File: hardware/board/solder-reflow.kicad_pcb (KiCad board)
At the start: 2 copper layers, 128.3 x 63.5 mm, 55 parts, among them J1 AC_Con, J2 OLED 0.91, J3 PTC_Con, J4 Barrel_Jack_Switch_Pin3Ring, K1 G3MB202PDC12, Q1 BC557, SW1 RotaryEncoder_Switch, U1 TL431LP, U2 OPA2134, U3 OPA2134, U4 L7805, U5 WeMos_D1_mini

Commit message: [6-7-1245] finish first layout, need to review
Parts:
- removed C4, C5: 10nF, Capacitor_THT:C_Disc_D4.3mm_W1.9mm_P5.00mm
- removed H3: MountingHole_Pad, MountingHole:MountingHole_3.2mm_M3_DIN965_Pad
- removed R11, R21: 10k, Resistor_THT:R_Axial_DIN0207_L6.3mm_D2.5mm_P10.16mm_Horizontal
- removed REF**: OSHW-Logo2_14.6x12mm_Copper, Symbol:OSHW-Logo2_14.6x12mm_Copper
- removed REF** (x2): ESD-Logo_8.9x8mm_SilkScreen, Symbol:ESD-Logo_8.9x8mm_SilkScreen
- removed REF**: Gauge_10mm_Type5_SilkScreenTop, Calibration_Scale:Gauge_10mm_Type5_SilkScreenTop
- removed SW1: RotaryEncoder_Switch, Rotary_Encoder:RotaryEncoder_Alps_EC11E-Switch_Vertical_H20mm
- removed U5: WeMos_D1_mini, Module:WEMOS_D1_mini_light
- added C10: 100nF, Capacitor_SMD:C_1206_3216Metric_Pad1.33x1.80mm_HandSolder, F.Cu at (128.5, 81.5)
- added C11: 100nF, Capacitor_SMD:C_1206_3216Metric_Pad1.33x1.80mm_HandSolder, B.Cu at (141.6, 77.0)
- added C12: 100nF, Capacitor_SMD:C_1206_3216Metric_Pad1.33x1.80mm_HandSolder, B.Cu at (150.1, 77.0)
- added C13: 22uF, Capacitor_SMD:C_1206_3216Metric_Pad1.33x1.80mm_HandSolder, B.Cu at (147.1, 77.0)
- added C14: 100nF, Capacitor_SMD:C_1206_3216Metric_Pad1.33x1.80mm_HandSolder, B.Cu at (110.2, 81.0)
- added C15: 100nF, Capacitor_SMD:C_1206_3216Metric_Pad1.33x1.80mm_HandSolder, B.Cu at (122.0, 81.0)
- added C16: 1uF, Capacitor_SMD:C_1206_3216Metric_Pad1.33x1.80mm_HandSolder, B.Cu at (117.0, 89.5)
- added C17: 1uF, Capacitor_SMD:C_1206_3216Metric_Pad1.33x1.80mm_HandSolder, B.Cu at (117.0, 98.0)
- added C18: 1uF, Capacitor_SMD:C_1206_3216Metric_Pad1.33x1.80mm_HandSolder, B.Cu at (117.0, 106.5)
- added C19: 1uF, Capacitor_SMD:C_1206_3216Metric_Pad1.33x1.80mm_HandSolder, B.Cu at (117.0, 114.9)
- added C8: 22uF, Capacitor_SMD:C_1206_3216Metric_Pad1.33x1.80mm_HandSolder, B.Cu at (159.9, 95.8)
- added C9: 22uF, Capacitor_SMD:C_1206_3216Metric_Pad1.33x1.80mm_HandSolder, B.Cu at (156.9, 95.8)
- added D4: 1N4001, Diode_SMD:D_SOD-123, F.Cu at (174.2, 94.8)
- added D5: SSR2, LED_SMD:LED_2010_5025Metric_Pad1.52x2.65mm_HandSolder, F.Cu at (156.6, 107.7)
- added D7: TXD, LED_SMD:LED_2010_5025Metric_Pad1.52x2.65mm_HandSolder, F.Cu at (160.1, 91.0)
- added D8: RXD, LED_SMD:LED_2010_5025Metric_Pad1.52x2.65mm_HandSolder, F.Cu at (160.1, 100.0)
- added J10: PINOUT, Connector_PinHeader_2.54mm:PinHeader_1x10_P2.54mm_Vertical, F.Cu at (165.1, 76.1)
- added J12: ST7789, Connector_PinSocket_2.54mm:PinSocket_1x07_P2.54mm_Vertical, F.Cu at (139.5, 101.5)
- added J13: JTAG10, Connector_PinHeader_2.54mm:PinHeader_2x05_P2.54mm_Vertical, F.Cu at (141.2, 109.8)
- added J5: SSROUT2, TerminalBlock_MetzConnect:TerminalBlock_MetzConnect_Type011_RT05502HBWC_1x02_P5.00mm_Horizontal, F.Cu at (182.7, 108.2)
- added J6: USB_B, Connector_USB:USB_B_OST_USB-B1HSxx_Horizontal, F.Cu at (112.0, 74.5)
- added J7: PINOUT, Connector_PinHeader_2.54mm:PinHeader_1x10_P2.54mm_Vertical, F.Cu at (136.3, 116.2)
- added J8: PINOUT, Connector_PinHeader_2.54mm:PinHeader_1x10_P2.54mm_Vertical, F.Cu at (132.1, 76.2)
- added J9: 12VIN, TerminalBlock_MetzConnect:TerminalBlock_MetzConnect_Type011_RT05502HBWC_1x02_P5.00mm_Horizontal, F.Cu at (182.8, 86.0)
- added Q2: SS8550, Package_TO_SOT_SMD:SOT-23_Handsoldering, F.Cu at (169.2, 94.5)
- added Q3: SS8050, Package_TO_SOT_SMD:SOT-23_Handsoldering, F.Cu at (127.0, 89.5)
- added Q4: SS8050, Package_TO_SOT_SMD:SOT-23_Handsoldering, F.Cu at (127.0, 97.0)
- added R23: 10k, Resistor_SMD:R_0805_2012Metric_Pad1.20x1.40mm_HandSolder, F.Cu at (168.5, 89.5)
- added R24: 10k, Resistor_SMD:R_0805_2012Metric_Pad1.20x1.40mm_HandSolder, F.Cu at (171.4, 89.5)
- added R25: 1k, Resistor_SMD:R_0805_2012Metric_Pad1.20x1.40mm_HandSolder, F.Cu at (174.5, 89.5)
- added R26: 1k, Resistor_SMD:R_0805_2012Metric_Pad1.20x1.40mm_HandSolder, B.Cu at (157.2, 84.2)
- added R27: 1k, Resistor_SMD:R_0805_2012Metric_Pad1.20x1.40mm_HandSolder, B.Cu at (159.8, 84.2)
- added R28: 1k, Resistor_SMD:R_0805_2012Metric_Pad1.20x1.40mm_HandSolder, B.Cu at (144.3, 76.3)
- added R29: 22k, Resistor_SMD:R_0805_2012Metric_Pad1.20x1.40mm_HandSolder, B.Cu at (128.5, 87.5)
- added R30: 22k, Resistor_SMD:R_0805_2012Metric_Pad1.20x1.40mm_HandSolder, B.Cu at (127.1, 82.0)
- added R31: 22k, Resistor_SMD:R_0805_2012Metric_Pad1.20x1.40mm_HandSolder, B.Cu at (127.5, 77.0)
- added R32: 22k, Resistor_SMD:R_0805_2012Metric_Pad1.20x1.40mm_HandSolder, B.Cu at (128.5, 96.0)
- added RA1: 25k, Resistor_SMD:R_0805_2012Metric_Pad1.20x1.40mm_HandSolder, F.Cu at (126.5, 109.5)
- added RB1: 25k, Resistor_SMD:R_0805_2012Metric_Pad1.20x1.40mm_HandSolder, F.Cu at (126.5, 112.0)
- added SW2: RST, Button_Switch_SMD:SW_SPST_B3S-1000, F.Cu at (110.2, 81.0)
- added SW3: IO0, Button_Switch_SMD:SW_SPST_B3S-1000, F.Cu at (122.0, 81.0)
- added SW4: IO0, Button_Switch_SMD:SW_SPST_B3S-1000, F.Cu at (117.0, 89.5)
- added SW5: IO0, Button_Switch_SMD:SW_SPST_B3S-1000, F.Cu at (117.0, 98.0)
- added SW6: IO0, Button_Switch_SMD:SW_SPST_B3S-1000, F.Cu at (117.0, 106.5)
- added SW7: IO0, Button_Switch_SMD:SW_SPST_B3S-1000, F.Cu at (117.0, 114.9)
- added U6: ESP32-WROOM-32D, RF_Module:ESP32-WROOM-32D, F.Cu at (147.1, 83.5)
- added U7: CH340C, Package_SO:SOIC-16_3.9x9.9mm_P1.27mm, B.Cu at (138.0, 85.5)
- C1: value 68nF -> 1nF; footprint Capacitor_THT:C_Disc_D4.3mm_W1.9mm_P5.00mm -> Capacitor_SMD:C_1206_3216Metric_Pad1.33x1.80mm_HandSolder
- C2: value 390nF -> 1uF; footprint Capacitor_THT:C_Disc_D4.3mm_W1.9mm_P5.00mm -> Capacitor_SMD:C_1206_3216Metric_Pad1.33x1.80mm_HandSolder; moved to B.Cu
- C3: value 180nF -> 1nF; footprint Capacitor_THT:C_Disc_D4.3mm_W1.9mm_P5.00mm -> Capacitor_SMD:C_1206_3216Metric_Pad1.33x1.80mm_HandSolder
- C6, C7: footprint Capacitor_THT:CP_Radial_D6.3mm_P2.50mm -> Capacitor_SMD:C_1206_3216Metric_Pad1.33x1.80mm_HandSolder; moved to B.Cu
- D1: footprint Diode_THT:D_DO-41_SOD81_P10.16mm_Horizontal -> Diode_SMD:D_SOD-123; moved to B.Cu
- D2: value SSR -> SSR1; footprint LED_THT:LED_D5.0mm -> LED_SMD:LED_2010_5025Metric_Pad1.52x2.65mm_HandSolder
- D3: footprint LED_THT:LED_D5.0mm -> LED_SMD:LED_2010_5025Metric_Pad1.52x2.65mm_HandSolder
- F1, K1, TH1, U4: moved to B.Cu
- J1: value AC_Con -> ACCON; footprint TerminalBlock_MetzConnect:TerminalBlock_MetzConnect_Type011_RT05502HBWC_1x02_P5.00mm_Horizontal -> TerminalBlock_MetzConnect:TerminalBlock_MetzConnect_Type055_RT01503HDWU_1x03_P5.00mm_Horizontal
- J4: value Barrel_Jack_Switch_Pin3Ring -> 12V
- Q1: value BC557 -> SS8550; footprint Package_TO_SOT_THT:TO-92_Inline_Wide -> Package_TO_SOT_SMD:SOT-23_Handsoldering; moved to B.Cu
- R1, R14, R15, R16, R17, R18, R19, R2, R20, R4, R5, R6: footprint Resistor_THT:R_Axial_DIN0207_L6.3mm_D2.5mm_P10.16mm_Horizontal -> Resistor_SMD:R_0805_2012Metric_Pad1.20x1.40mm_HandSolder; moved to B.Cu
- R10: value 5.1K -> 10k; footprint Resistor_THT:R_Axial_DIN0207_L6.3mm_D2.5mm_P10.16mm_Horizontal -> Resistor_SMD:R_0805_2012Metric_Pad1.20x1.40mm_HandSolder
- R12: value 3.09k -> 4K7; footprint Resistor_THT:R_Axial_DIN0207_L6.3mm_D2.5mm_P10.16mm_Horizontal -> Resistor_SMD:R_0805_2012Metric_Pad1.20x1.40mm_HandSolder; moved to B.Cu
- R13: value 20k -> 4K7; footprint Resistor_THT:R_Axial_DIN0207_L6.3mm_D2.5mm_P10.16mm_Horizontal -> Resistor_SMD:R_0805_2012Metric_Pad1.20x1.40mm_HandSolder; moved to B.Cu
- R22, R3: footprint Resistor_THT:R_Axial_DIN0207_L6.3mm_D2.5mm_P10.16mm_Horizontal -> Resistor_SMD:R_0805_2012Metric_Pad1.20x1.40mm_HandSolder
- R7: value 1k -> 10k; footprint Resistor_THT:R_Axial_DIN0207_L6.3mm_D2.5mm_P10.16mm_Horizontal -> Resistor_SMD:R_0805_2012Metric_Pad1.20x1.40mm_HandSolder
- R8: value 17.4k -> 16k; footprint Resistor_THT:R_Axial_DIN0207_L6.3mm_D2.5mm_P10.16mm_Horizontal -> Resistor_SMD:R_0805_2012Metric_Pad1.20x1.40mm_HandSolder
- R9: value 107k -> 16k; footprint Resistor_THT:R_Axial_DIN0207_L6.3mm_D2.5mm_P10.16mm_Horizontal -> Resistor_SMD:R_0805_2012Metric_Pad1.20x1.40mm_HandSolder
- U2: value OPA2134 -> TL074; footprint Package_DIP:DIP-8_W7.62mm_LongPads -> Package_SO:SOIC-14_3.9x8.7mm_P1.27mm; moved to B.Cu
- U3: value OPA2134 -> AMS1117-3.3; footprint Package_DIP:DIP-8_W7.62mm_LongPads -> Package_TO_SOT_SMD:SOT-223-3_TabPin2; moved to B.Cu
- moved J3 84.4 mm to (182.7, 97.2)
- moved H4 75.4 mm to (169.5, 117.0)
- moved TH1 75.3 mm to (165.2, 102.0)
- moved R1 54.0 mm to (126.6, 111.0), turned to 180 degrees
- moved C1 53.8 mm to (131.8, 105.0), turned to -90 degrees
- moved R13 53.3 mm to (145.1, 87.0), turned to 180 degrees
- moved R8 52.4 mm to (126.5, 104.5), turned to 180 degrees
- moved R12 50.0 mm to (145.1, 89.5), turned to 180 degrees
- moved U3 48.8 mm to (152.2, 85.8), turned to 90 degrees
- moved U2 48.3 mm to (133.5, 106.5), turned to 180 degrees
- moved H2 46.7 mm to (171.5, 78.5)
- moved J1 46.6 mm to (183.0, 125.8), turned to 90 degrees
- moved C7 45.3 mm to (157.6, 89.2), turned to -90 degrees
- moved R4 45.2 mm to (126.6, 106.0), turned to 180 degrees
- moved R3 44.1 mm to (126.5, 102.0), turned to 180 degrees
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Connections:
- net /pt100_out renamed /PT100Voltage
- net Net-(U4-IN) renamed +12V
- C1 pad 1: Net-(C1-Pad1) -> Net-(U2D-+)
- C2 pad 1: Net-(C1-Pad2) -> +3.3V
- C3 pad 1: Net-(U3A-+) -> Net-(U2C-+)
- F1 pad 1: Net-(K1-L2) -> AC
- F1 pad 2: AC -> Net-(K1-L2)
- J1 pad 2: Net-(J1-Pin_2) -> unconnected-(J1-Pin_2-Pad2)
- J2 pad 1: /OLED_SCL -> /I2C_SDA
- J2 pad 2: /OLED_SDA -> /I2C_SCL
- K1 pad 1: Net-(J1-Pin_2) -> Net-(J1-Pin_3)
- Q1 pad 1: Net-(K1-+) -> Net-(Q1-B)
- Q1 pad 2: Net-(Q1-B) -> Net-(D1-K)
- Q1 pad 3: Net-(D1-K) -> Net-(K1-+)
- R1 pad 1: +5V -> +2V5
- R1 pad 2: +2V5 -> +5V
- R10 pad 1: Net-(R10-Pad1) -> Net-(Q4-B)
- R10 pad 2: Net-(U3B-+) -> /RTS
- R12 pad 1: GND -> /I2C_SDA
- R12 pad 2: Net-(U3A--) -> +3.3V
- R13 pad 1: Net-(U3A--) -> /I2C_SCL
- R13 pad 2: Net-(R10-Pad1) -> +3.3V
- R15 pad 1: /SSR_in -> /SSRIN1
- R16 pad 1: Net-(R16-Pad1) -> +3.3V
- R16 pad 2: +5V -> Net-(R16-Pad2)
- R17 pad 1: Net-(R17-Pad1) -> +3.3V
- R17 pad 2: +5V -> Net-(R17-Pad2)
- R19 pad 1: /ENC_SW -> +3.3V
- R19 pad 2: +5V -> Net-(R19-Pad2)
- R20 pad 1: Net-(R16-Pad1) -> +3.3V
- R20 pad 2: /ENC_A -> Net-(R20-Pad2)
- R7 pad 1: Net-(R10-Pad1) -> Net-(Q3-B)
- R7 pad 2: Net-(C1-Pad1) -> /DTR
- R9 pad 1: Net-(U3A-+) -> Net-(U2C-+)
- U2 pad 4: GND -> +5V
- U2 pad 8: +5V -> Net-(U2D-+)
- U3 pad 1: Net-(R10-Pad1) -> GND
- U3 pad 2: Net-(U3A--) -> +3.3V
- U3 pad 3: Net-(U3A-+) -> +5V
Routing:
- net GND: track 364.4 -> 0.00 mm, vias 4 -> 0
- net +5V: track 144.5 -> 0.00 mm, vias 4 -> 0
- net /PT100Voltage: track 106.3 -> 0.00 mm, vias 2 -> 0
- net /Sallen-Key_out: track 100.6 -> 0.00 mm, vias 2 -> 0
- net /ENC_SW: track 89.3 -> 0.00 mm, vias 2 -> 0
- net /ENC_A: track 76.9 -> 0.00 mm, vias 2 -> 0
- net /OLED_SDA: track 71.7 -> 0.00 mm, vias 2 -> 0
- net Net-(R10-Pad1): track 68.5 -> 0.00 mm
- net /OLED_SCL: track 66.8 -> 0.00 mm, vias 2 -> 0
- net /ENC_B: track 65.8 -> 0.00 mm, vias 2 -> 0
- net Net-(R16-Pad1): track 64.2 -> 0.00 mm, vias 2 -> 0
- net Net-(U3A-+): track 43.1 -> 0.00 mm
- net Net-(R3-Pad2): track 39.0 -> 0.00 mm
- net +2V5: track 37.8 -> 0.00 mm
- net +12V: track 34.1 -> 0.00 mm
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- removed copper zone on F.Cu, net +5V
- removed copper zone on B.Cu, net GND
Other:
- board size 128.3 x 63.5 mm -> 86 x 65 mm
- board text added: "SORE V2"
- board text removed: "06-03-2024"
- board text removed: "220V"
- board text removed: "SORE"
- board text removed: "Solder Reflow"
- board text removed: "V1 Custom PTC Heater Controller for SMD Solder-Reflow"
- board text removed: "Warning"

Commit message: [8-06-0716] finish up layout plus adding several random graphic
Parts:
- removed J12: ST7789, Connector_PinSocket_2.54mm:PinSocket_1x07_P2.54mm_Vertical
- added J11: ST7789, Connector_PinSocket_2.54mm:PinSocket_1x08_P2.54mm_Vertical, F.Cu at (139.1, 102.0)
- C1, C10, C11, C12, C13, C14, C15, C16, C17, C18, C19, C2, C3, C6, C7, C8, C9: footprint Capacitor_SMD:C_1206_3216Metric_Pad1.33x1.80mm_HandSolder -> Capacitor_SMD:C_0805_2012Metric_Pad1.18x1.45mm_HandSolder
- D2, D3, D5, D7, D8: footprint LED_SMD:LED_2010_5025Metric_Pad1.52x2.65mm_HandSolder -> LED_SMD:LED_1206_3216Metric_Pad1.42x1.75mm_HandSolder
- J1: footprint TerminalBlock_MetzConnect:TerminalBlock_MetzConnect_Type055_RT01503HDWU_1x03_P5.00mm_Horizontal -> TerminalBlock_Phoenix:TerminalBlock_Phoenix_PT-1,5-3-5.0-H_1x03_P5.00mm_Horizontal
- J3, J5, J9: footprint TerminalBlock_MetzConnect:TerminalBlock_MetzConnect_Type011_RT05502HBWC_1x02_P5.00mm_Horizontal -> TerminalBlock_Phoenix:TerminalBlock_Phoenix_PT-1,5-2-5.0-H_1x02_P5.00mm_Horizontal
- SW2, SW3: footprint Button_Switch_SMD:SW_SPST_B3S-1000 -> Button_Switch_SMD:SW_Push_1P1T_NO_6x6mm_H9.5mm
- SW4: value IO0 -> D; footprint Button_Switch_SMD:SW_SPST_B3S-1000 -> Button_Switch_SMD:SW_Push_1P1T_NO_6x6mm_H9.5mm
- SW5: value IO0 -> U; footprint Button_Switch_SMD:SW_SPST_B3S-1000 -> Button_Switch_SMD:SW_Push_1P1T_NO_6x6mm_H9.5mm
- SW6: value IO0 -> L; footprint Button_Switch_SMD:SW_SPST_B3S-1000 -> Button_Switch_SMD:SW_Push_1P1T_NO_6x6mm_H9.5mm
- SW7: value IO0 -> R; footprint Button_Switch_SMD:SW_SPST_B3S-1000 -> Button_Switch_SMD:SW_Push_1P1T_NO_6x6mm_H9.5mm
- TH1: moved to F.Cu
- moved D2 9.37 mm to (163.9, 116.3)
- moved D5 9.37 mm to (160.5, 116.2)
- moved J7 9.33 mm to (137.6, 107.0)
- moved J13 7.61 mm to (142.4, 117.3)
- moved C10 6.26 mm to (125.5, 76.0), turned to 0 degrees
- moved D8 4.67 mm to (156.5, 97.0)
- moved J8 2.09 mm to (130.0, 76.1)
- moved TH1 1.95 mm to (166.5, 103.5), turned to 180 degrees
- moved R1 1.59 mm to (125.0, 111.0)
- moved R2 1.59 mm to (125.0, 108.5)
- moved R4 1.59 mm to (125.0, 106.0)
- moved R5 1.59 mm to (125.0, 103.5)
- moved R6 1.59 mm to (125.0, 101.0)
- moved Q3 1.58 mm to (125.5, 90.0)
- moved Q4 1.58 mm to (125.5, 97.5)
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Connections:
- net /IO2 renamed /LCD_CS
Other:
- board text added: "3V3"
- board text added: "5V"
- board text added: "8 JUNI 06:37 WIB"
- board text added: "ADC1_CH7"
- board text added: "GND"
- board text added: "I2C_SCL"
- board text added: "I2C_SDA"
- board text added: "IN1"
- board text added: "IN2"
- board text added: "IN3"
- board text added: "IN4"
- board text added: "IO0"
- board text added: "LCD_CS"
- board text added: "LCD_DC"
- board text added: "LCD_RST"
- board text added: "MTCK"
- board text added: "MTDI"
- board text added: "MTDO"
- board text added: "MTMS"
- board text added: "PT100"
- board text added: "RXD"
- board text added: "SORE Solder Reflow"
- board text added: "SSRIN1"
- board text added: "SSRIN2"
- board text added: "TXD"
- board text added: "VSPI_CLK"
- board text added: "VSPI_CS0"
- board text added: "VSPI_D"
- board text added: "VSPI_Q"
- board text added: "github.com/ahsanu123"

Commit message: [8-06-1357] finish routing, next do second review
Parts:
- moved J10 36.5 mm to (130.0, 76.1)
- moved J8 36.5 mm to (166.5, 76.1)
- moved R20 1.00 mm to (125.0, 96.0)
- moved R32 1.00 mm to (127.5, 96.0)
- moved R16 0.75 mm to (125.2, 87.5)
- moved R29 0.75 mm to (127.8, 87.5)
- turned C1 to 90 degrees
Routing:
- net GND: track 0.00 -> 473.7 mm, vias 0 -> 23
- net +5V: track 0.00 -> 219.8 mm, vias 0 -> 18
- net /EN: track 0.00 -> 168.8 mm, vias 0 -> 8
- net +3.3V: track 0.00 -> 164.9 mm, vias 0 -> 11
- net /IO0: track 0.00 -> 128.2 mm, vias 0 -> 17
- net /IN4: track 0.00 -> 122.7 mm, vias 0 -> 5
- net /PT100Voltage: track 0.00 -> 85.5 mm, vias 0 -> 2
- net /MTDI: track 0.00 -> 69.0 mm, vias 0 -> 3
- net /RXD: track 0.00 -> 60.7 mm, vias 0 -> 3
- net /VSPI_D: track 0.00 -> 56.6 mm, vias 0 -> 3
- net /VSPI_CLK: track 0.00 -> 54.7 mm, vias 0 -> 4
- net /MTCK: track 0.00 -> 52.5 mm, vias 0 -> 2
- net Net-(J1-Pin_3): track 0.00 -> 52.2 mm
- net /SSRIN2: track 0.00 -> 49.9 mm, vias 0 -> 4
- net /LCD_RST: track 0.00 -> 48.9 mm, vias 0 -> 5
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- added copper zone on F.Cu, net (none)
- added copper zone on B.Cu, net GND
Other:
- board text added: "Made With Love By Ah"

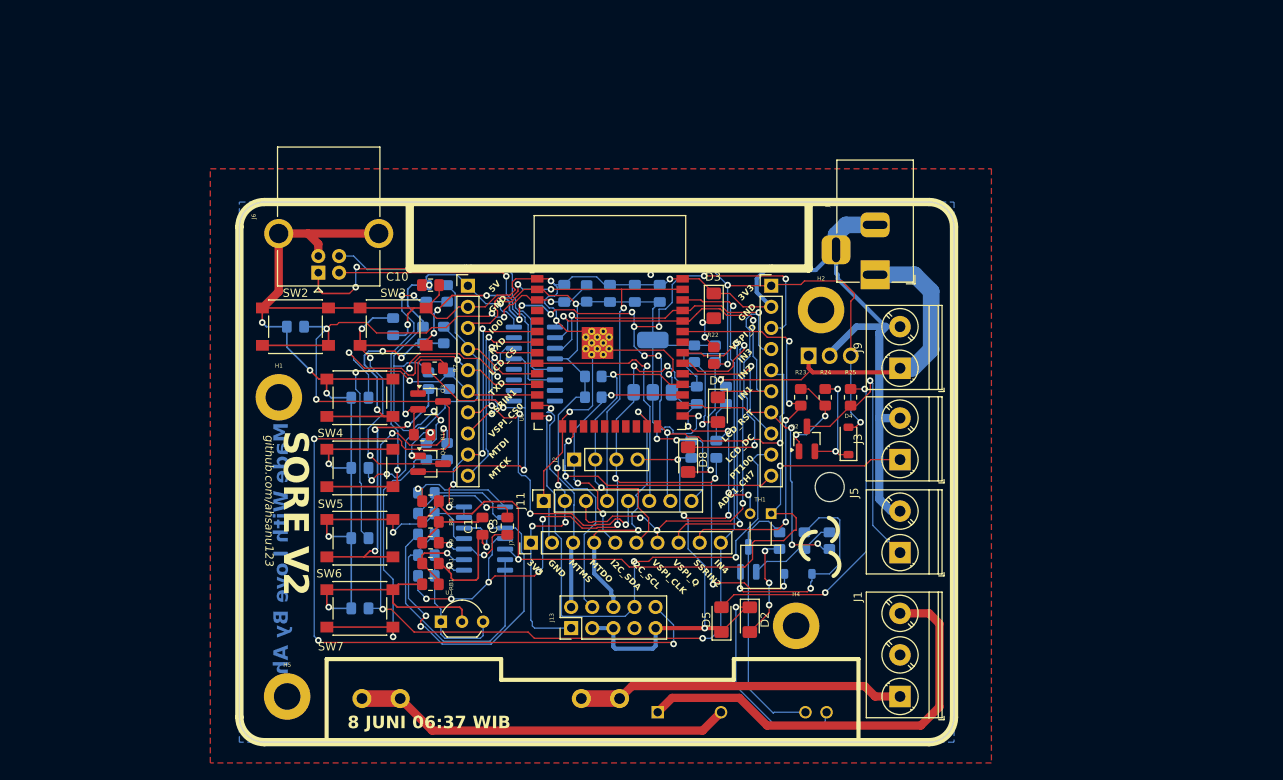
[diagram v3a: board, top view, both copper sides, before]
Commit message: [10-06-2138] tune silkscreen and track width
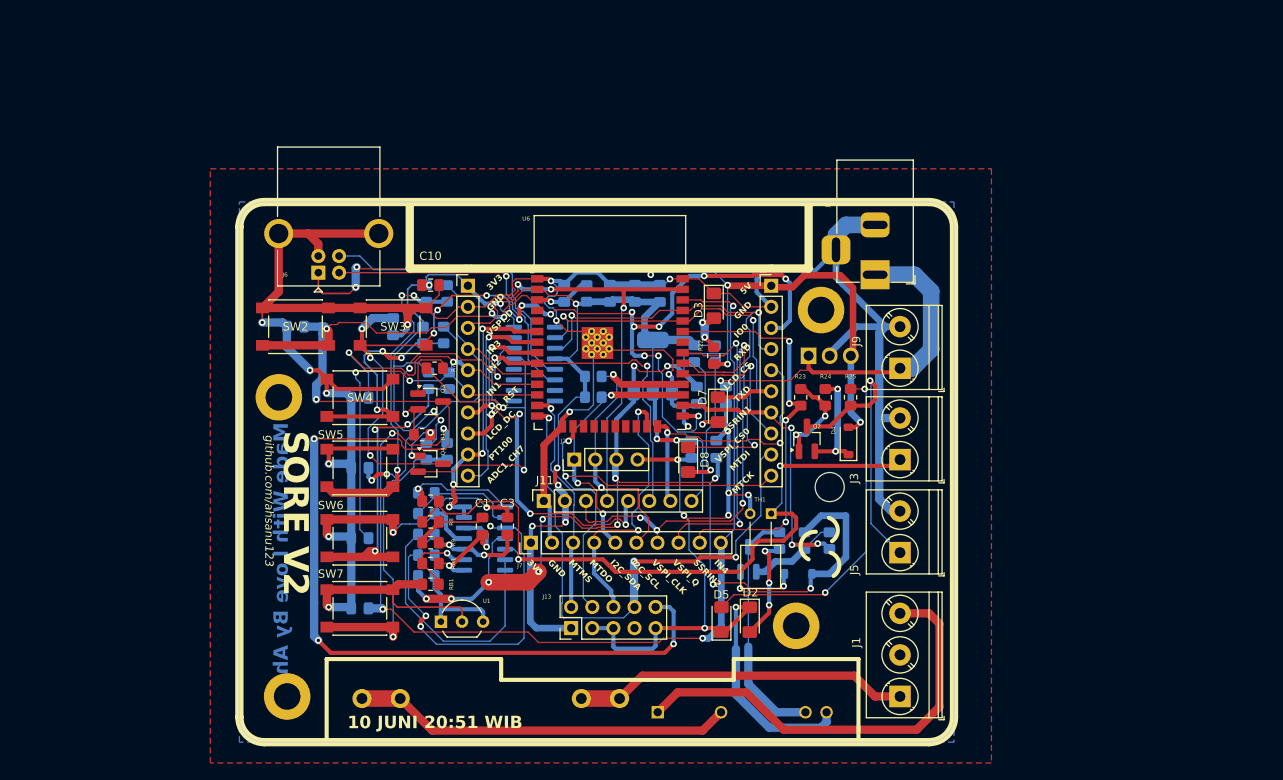
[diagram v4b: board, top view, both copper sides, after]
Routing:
- net /VSPI_D: track 56.6 -> 72.5 mm
- net GND: track 473.7 -> 482.1 mm
- net Net-(U2D-+): track 20.7 -> 15.1 mm
- net /EN: track 168.8 -> 173.1 mm
- net +3.3V: track 164.9 -> 169.2 mm
- net +5V: track 219.8 -> 223.4 mm
- net Net-(K1-+): track 31.8 -> 29.3 mm
- net /IN2: track 38.7 -> 40.8 mm
- net Net-(U2A-+): track 42.5 -> 44.6 mm
- net Net-(D1-K): track 26.9 -> 28.4 mm
- net /IO0: track 128.2 -> 126.8 mm
- net Net-(J5-Pin_1): track 32.9 -> 34.2 mm
- net Net-(J6-D-): track 37.3 -> 36.0 mm
- net /LCD_DC: track 47.3 -> 48.5 mm
- net AC: track 39.5 -> 40.5 mm
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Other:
- board text added: "10 JUNI 20:51 WIB"
- board text removed: "8 JUNI 06:37 WIB"

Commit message: [15-06-1731] adding gerber
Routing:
- net +5V: track 223.4 -> 222.0 mm
